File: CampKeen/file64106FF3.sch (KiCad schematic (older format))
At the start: 9 parts

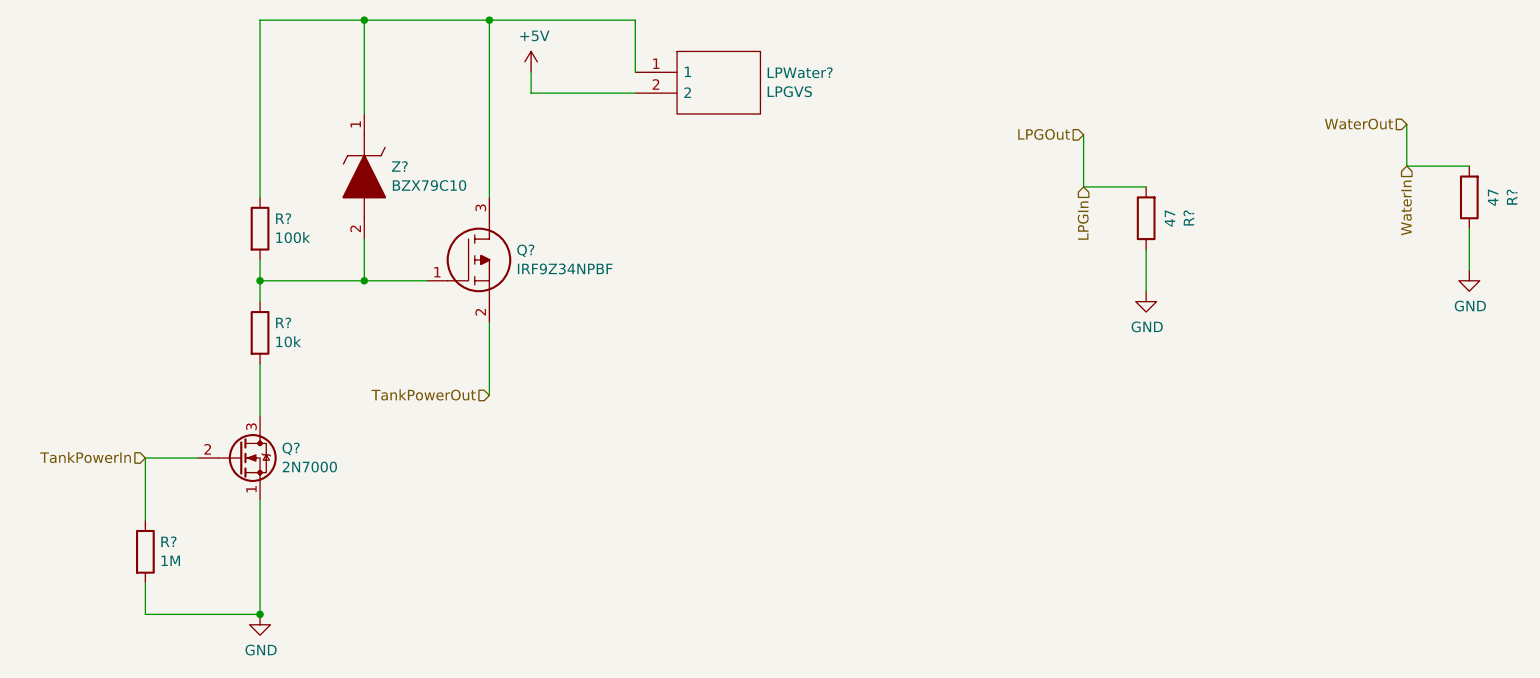
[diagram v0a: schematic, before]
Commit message: updated the pin mapping to the terms. cleaned up the Schematic. PCB placement and routing is what is left to do.
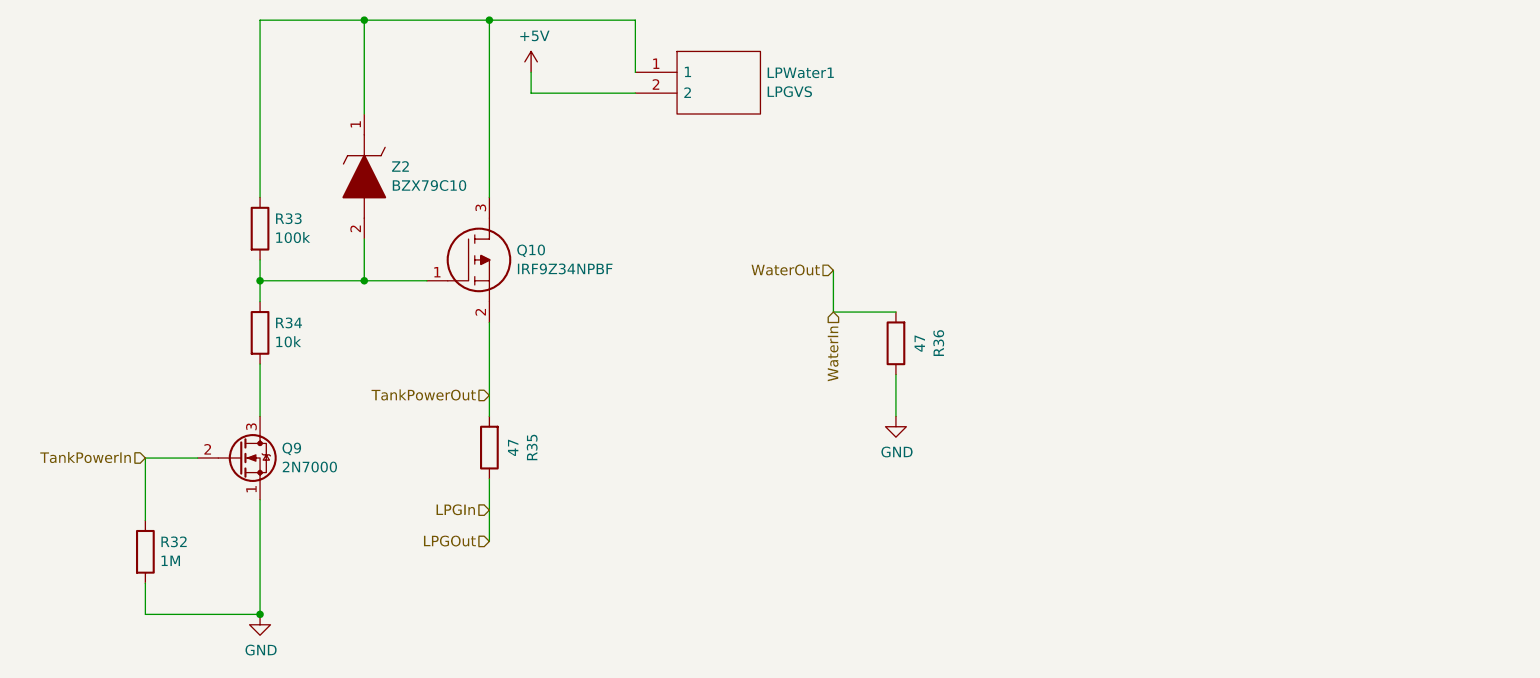
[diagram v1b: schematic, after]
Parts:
- Q10: renamed from Q?; footprint TO254P469X1042X1967-3P -> SamacSys_Parts:TO254P469X1042X1967-3P
- Z2: renamed from Z?; footprint DIOAD1068W53L380D172 -> SamacSys_Parts:DIOAD1068W53L380D172
- gave numbers to parts that had none: 7
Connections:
- net GND: no longer R35.1
- net LPGIn: now also R35.1; no longer R35.2
- net TankPowerOut: now also R35.2
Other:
- moved on the sheet: R35, R36
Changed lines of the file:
@@
 $Descr A4 11693 8268
 encoding utf-8
-Sheet 4 8
+Sheet 4 9
 Title ""
 Date ""
@@
 P 4000 2250
 AR Path="/641A2399" Ref="#PWR?"  Part="1"
-AR Path="/64106FF4/641A2399" Ref="#PWR?"  Part="1"
-F 0 "#PWR?" H 4000 2100 50  0001 C CNN
+AR Path="/64106FF4/641A2399" Ref="#PWR078"  Part="1"
+F 0 "#PWR078" H 4000 2100 50  0001 C CNN
 F 1 "+5V" H 4015 2423 50  0000 C CNN
 F 2 "" H 4000 2250 50  0001 C CNN
@@
 P 4500 2250
 AR Path="/641A23A6" Ref="LPWater?"  Part="1"
-AR Path="/64106FF4/641A23A6" Ref="LPWater?"  Part="1"
-F 0 "LPWater?" H 5128 2246 50  0000 L CNN
+AR Path="/64106FF4/641A23A6" Ref="LPWater1"  Part="1"
+F 0 "LPWater1" H 5128 2246 50  0000 L CNN
 F 1 "LPGVS" H 5128 2155 50  0000 L CNN
 F 2 "SamacSys_Parts:BK_HTC-15M" H 5150 2350 50  0001 L CNN
@@
 P 3500 3250
 AR Path="/62665296/641A23B2" Ref="Q?"  Part="1"
-AR Path="/64106FF4/641A23B2" Ref="Q?"  Part="1"
-F 0 "Q?" H 3930 3396 50  0000 L CNN
+AR Path="/64106FF4/641A23B2" Ref="Q10"  Part="1"
+F 0 "Q10" H 3930 3396 50  0000 L CNN
 F 1 "IRF9Z34NPBF" H 3930 3305 50  0000 L CNN
-F 2 "TO254P469X1042X1967-3P" H 3950 3200 50  0001 L CNN
+F 2 "SamacSys_Parts:TO254P469X1042X1967-3P" H 3950 3200 50  0001 L CNN
 F 3 "https://www.infineon.com/dgdl/irf9z34npbf.pdf?fileId=5546d462533600a40153561220af1ddd" H 3950 3100 50  0001 L CNN
 F 4 "MOSFET MOSFT PCh -55V -17A 100mOhm 23.3nC" H 3950 3000 50  0001 L CNN "Description"
@@
 P 2150 4550
 AR Path="/62665296/641A23B8" Ref="R?"  Part="1"
-AR Path="/64106FF4/641A23B8" Ref="R?"  Part="1"
-F 0 "R?" H 2220 4596 50  0000 L CNN
+AR Path="/64106FF4/641A23B8" Ref="R32"  Part="1"
+F 0 "R32" H 2220 4596 50  0000 L CNN
 F 1 "1M" H 2220 4505 50  0000 L CNN
 F 2 "Resistor_THT:R_Axial_DIN0207_L6.3mm_D2.5mm_P2.54mm_Vertical" V 2080 4550 50  0001 C CNN
@@
 P 2700 4850
 AR Path="/62665296/641A23BE" Ref="#PWR?"  Part="1"
-AR Path="/64106FF4/641A23BE" Ref="#PWR?"  Part="1"
-F 0 "#PWR?" H 2700 4600 50  0001 C CNN
+AR Path="/64106FF4/641A23BE" Ref="#PWR077"  Part="1"
+F 0 "#PWR077" H 2700 4600 50  0001 C CNN
 F 1 "GND" H 2705 4677 50  0000 C CNN
 F 2 "" H 2700 4850 50  0001 C CNN
@@
 P 2600 4100
 AR Path="/62665296/641A23C9" Ref="Q?"  Part="1"
-AR Path="/64106FF4/641A23C9" Ref="Q?"  Part="1"
-F 0 "Q?" H 2804 4146 50  0000 L CNN
+AR Path="/64106FF4/641A23C9" Ref="Q9"  Part="1"
+F 0 "Q9" H 2804 4146 50  0000 L CNN
 F 1 "2N7000" H 2804 4055 50  0000 L CNN
 F 2 "Package_TO_SOT_THT:TO-92_Inline" H 2800 4025 50  0001 L CIN
@@
 P 2700 3000
 AR Path="/62665296/641A23D0" Ref="R?"  Part="1"
-AR Path="/64106FF4/641A23D0" Ref="R?"  Part="1"
-F 0 "R?" H 2770 3046 50  0000 L CNN
+AR Path="/64106FF4/641A23D0" Ref="R33"  Part="1"
+F 0 "R33" H 2770 3046 50  0000 L CNN
 F 1 "100k" H 2770 2955 50  0000 L CNN
 F 2 "Resistor_THT:R_Axial_DIN0207_L6.3mm_D2.5mm_P2.54mm_Vertical" V 2630 3000 50  0001 C CNN
@@
 P 2700 3500
 AR Path="/62665296/641A23D6" Ref="R?"  Part="1"
-AR Path="/64106FF4/641A23D6" Ref="R?"  Part="1"
-F 0 "R?" H 2770 3546 50  0000 L CNN
+AR Path="/64106FF4/641A23D6" Ref="R34"  Part="1"
+F 0 "R34" H 2770 3546 50  0000 L CNN
 F 1 "10k" H 2770 3455 50  0000 L CNN
 F 2 "Resistor_THT:R_Axial_DIN0207_L6.3mm_D2.5mm_P2.54mm_Vertical" V 2630 3500 50  0001 C CNN
@@
 P 3200 2450
 AR Path="/62665296/641A23E2" Ref="Z?"  Part="1"
-AR Path="/64106FF4/641A23E2" Ref="Z?"  Part="1"
-F 0 "Z?" V 3454 2320 50  0000 R CNN
+AR Path="/64106FF4/641A23E2" Ref="Z2"  Part="1"
+F 0 "Z2" V 3454 2320 50  0000 R CNN
 F 1 "BZX79C10" V 3545 2320 50  0000 R CNN
-F 2 "DIOAD1068W53L380D172" H 3600 2600 50  0001 L CNN
+F 2 "SamacSys_Parts:DIOAD1068W53L380D172" H 3600 2600 50  0001 L CNN
 F 3 "https://www.fairchildsemi.com/datasheets/BZ/BZX79C10.pdf" H 3600 2500 50  0001 L CNN
 F 4 "BZX79C10, Zener Diode, 10V +/-5 500 mW 0.2A, 2-Pin DO-35" H 3600 2400 50  0001 L CNN "Description"
@@
 	3200 2000 2700 2000
 Wire Wire Line
-	3800 3800 3800 3450
-Wire Wire Line
 	3800 2000 4500 2000
 Wire Wire Line
@@
 TankPowerOut
 $Comp
-L Device:R R?
+L Device:R R35
 U 1 1 643133F3
-P 6950 2950
-F 0 "R?" V 6743 2950 50  0000 C CNN
-F 1 "47" V 6834 2950 50  0000 C CNN
-F 2 "Resistor_THT:R_Axial_DIN0207_L6.3mm_D2.5mm_P2.54mm_Vertical" V 6880 2950 50  0001 C CNN
-F 3 "~" H 6950 2950 50  0001 C CNN
-	1    6950 2950
+P 3800 4050
+F 0 "R35" V 3593 4050 50  0000 C CNN
+F 1 "47" V 3684 4050 50  0000 C CNN
+F 2 "Resistor_THT:R_Axial_DIN0207_L6.3mm_D2.5mm_P2.54mm_Vertical" V 3730 4050 50  0001 C CNN
+F 3 "~" H 3800 4050 50  0001 C CNN
+	1    3800 4050
 	-1   0    0    1
 $EndComp
 $Comp
-L power:GND #PWR?
-U 1 1 643133F9
-P 6950 3300
-F 0 "#PWR?" H 6950 3050 50  0001 C CNN
-F 1 "GND" H 6955 3127 50  0000 C CNN
-F 2 "" H 6950 3300 50  0001 C CNN
-F 3 "" H 6950 3300 50  0001 C CNN
-	1    6950 3300
-	1    0    0    -1
-$EndComp
-Wire Wire Line
-	6950 3100 6950 3300
-$Comp
-L Device:R R?
+L Device:R R36
 U 1 1 64313403
-P 8500 2850
-F 0 "R?" V 8293 2850 50  0000 C CNN
-F 1 "47" V 8384 2850 50  0000 C CNN
-F 2 "Resistor_THT:R_Axial_DIN0207_L6.3mm_D2.5mm_P2.54mm_Vertical" V 8430 2850 50  0001 C CNN
-F 3 "~" H 8500 2850 50  0001 C CNN
-	1    8500 2850
+P 5750 3550
+F 0 "R36" V 5543 3550 50  0000 C CNN
+F 1 "47" V 5634 3550 50  0000 C CNN
+F 2 "Resistor_THT:R_Axial_DIN0207_L6.3mm_D2.5mm_P2.54mm_Vertical" V 5680 3550 50  0001 C CNN
+F 3 "~" H 5750 3550 50  0001 C CNN
+	1    5750 3550
 	-1   0    0    1
 $EndComp
 $Comp
-L power:GND #PWR?
+L power:GND #PWR079
 U 1 1 64313409
-P 8500 3200
-F 0 "#PWR?" H 8500 2950 50  0001 C CNN
-F 1 "GND" H 8505 3027 50  0000 C CNN
-F 2 "" H 8500 3200 50  0001 C CNN
-F 3 "" H 8500 3200 50  0001 C CNN
-	1    8500 3200
-	1    0    0    -1
-$EndComp
-Wire Wire Line
-	8500 3000 8500 3200
-Text HLabel 6650 2800 3    50   Input ~ 0
+P 5750 3900
+F 0 "#PWR079" H 5750 3650 50  0001 C CNN
+F 1 "GND" H 5755 3727 50  0000 C CNN
+F 2 "" H 5750 3900 50  0001 C CNN
+F 3 "" H 5750 3900 50  0001 C CNN
+	1    5750 3900
+	1    0    0    -1
+$EndComp
+Wire Wire Line
+	5750 3700 5750 3900
+Text HLabel 3800 4350 0    50   Input ~ 0
 LPGIn
-Text HLabel 8200 2700 3    50   Input ~ 0
+Text HLabel 5450 3400 3    50   Input ~ 0
 WaterIn
-Text HLabel 8200 2500 0    50   Input ~ 0
+Text HLabel 5450 3200 0    50   Input ~ 0
 WaterOut
-Text HLabel 6650 2550 0    50   Input ~ 0
+Text HLabel 3800 4500 0    50   Input ~ 0
 LPGOut
 Wire Wire Line
-	6950 2800 6650 2800
-Wire Wire Line
-	6650 2550 6650 2800
-Wire Wire Line
-	8200 2500 8200 2700
-Wire Wire Line
-	8500 2700 8200 2700
+	5450 3200 5450 3400
+Wire Wire Line
+	5750 3400 5450 3400
+Wire Wire Line
+	3800 4200 3800 4500
+Wire Wire Line
+	3800 3450 3800 3900
 $EndSCHEMATC

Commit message: separated the 12 and 5 volt outputs. added another spare output.
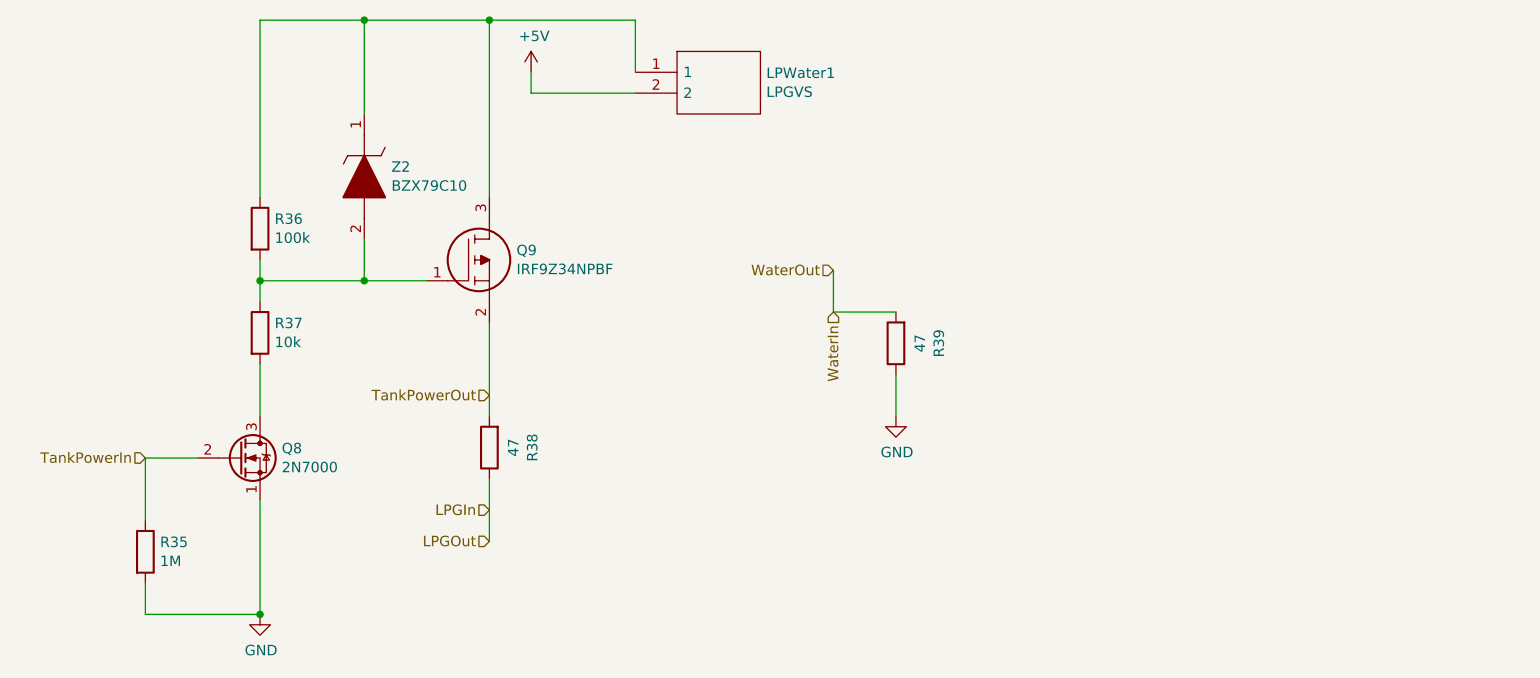
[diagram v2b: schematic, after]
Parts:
- renumbered Q9 to Q8, Q10 to Q9, R32 to R35, R33 to R36, R34 to R37, R35 to R38, R36 to R39
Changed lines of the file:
@@
 $Descr A4 11693 8268
 encoding utf-8
-Sheet 4 9
+Sheet 4 10
 Title ""
 Date ""
@@
 P 4000 2250
 AR Path="/641A2399" Ref="#PWR?"  Part="1"
-AR Path="/64106FF4/641A2399" Ref="#PWR078"  Part="1"
-F 0 "#PWR078" H 4000 2100 50  0001 C CNN
+AR Path="/64106FF4/641A2399" Ref="#PWR085"  Part="1"
+F 0 "#PWR085" H 4000 2100 50  0001 C CNN
 F 1 "+5V" H 4015 2423 50  0000 C CNN
 F 2 "" H 4000 2250 50  0001 C CNN
@@
 P 3500 3250
 AR Path="/62665296/641A23B2" Ref="Q?"  Part="1"
-AR Path="/64106FF4/641A23B2" Ref="Q10"  Part="1"
-F 0 "Q10" H 3930 3396 50  0000 L CNN
+AR Path="/64106FF4/641A23B2" Ref="Q9"  Part="1"
+F 0 "Q9" H 3930 3396 50  0000 L CNN
 F 1 "IRF9Z34NPBF" H 3930 3305 50  0000 L CNN
 F 2 "SamacSys_Parts:TO254P469X1042X1967-3P" H 3950 3200 50  0001 L CNN
@@
 P 2150 4550
 AR Path="/62665296/641A23B8" Ref="R?"  Part="1"
-AR Path="/64106FF4/641A23B8" Ref="R32"  Part="1"
-F 0 "R32" H 2220 4596 50  0000 L CNN
+AR Path="/64106FF4/641A23B8" Ref="R35"  Part="1"
+F 0 "R35" H 2220 4596 50  0000 L CNN
 F 1 "1M" H 2220 4505 50  0000 L CNN
 F 2 "Resistor_THT:R_Axial_DIN0207_L6.3mm_D2.5mm_P2.54mm_Vertical" V 2080 4550 50  0001 C CNN
@@
 P 2700 4850
 AR Path="/62665296/641A23BE" Ref="#PWR?"  Part="1"
-AR Path="/64106FF4/641A23BE" Ref="#PWR077"  Part="1"
-F 0 "#PWR077" H 2700 4600 50  0001 C CNN
+AR Path="/64106FF4/641A23BE" Ref="#PWR084"  Part="1"
+F 0 "#PWR084" H 2700 4600 50  0001 C CNN
 F 1 "GND" H 2705 4677 50  0000 C CNN
 F 2 "" H 2700 4850 50  0001 C CNN
@@
 P 2600 4100
 AR Path="/62665296/641A23C9" Ref="Q?"  Part="1"
-AR Path="/64106FF4/641A23C9" Ref="Q9"  Part="1"
-F 0 "Q9" H 2804 4146 50  0000 L CNN
+AR Path="/64106FF4/641A23C9" Ref="Q8"  Part="1"
+F 0 "Q8" H 2804 4146 50  0000 L CNN
 F 1 "2N7000" H 2804 4055 50  0000 L CNN
 F 2 "Package_TO_SOT_THT:TO-92_Inline" H 2800 4025 50  0001 L CIN
@@
 P 2700 3000
 AR Path="/62665296/641A23D0" Ref="R?"  Part="1"
-AR Path="/64106FF4/641A23D0" Ref="R33"  Part="1"
-F 0 "R33" H 2770 3046 50  0000 L CNN
+AR Path="/64106FF4/641A23D0" Ref="R36"  Part="1"
+F 0 "R36" H 2770 3046 50  0000 L CNN
 F 1 "100k" H 2770 2955 50  0000 L CNN
 F 2 "Resistor_THT:R_Axial_DIN0207_L6.3mm_D2.5mm_P2.54mm_Vertical" V 2630 3000 50  0001 C CNN
@@
 P 2700 3500
 AR Path="/62665296/641A23D6" Ref="R?"  Part="1"
-AR Path="/64106FF4/641A23D6" Ref="R34"  Part="1"
-F 0 "R34" H 2770 3546 50  0000 L CNN
+AR Path="/64106FF4/641A23D6" Ref="R37"  Part="1"
+F 0 "R37" H 2770 3546 50  0000 L CNN
 F 1 "10k" H 2770 3455 50  0000 L CNN
 F 2 "Resistor_THT:R_Axial_DIN0207_L6.3mm_D2.5mm_P2.54mm_Vertical" V 2630 3500 50  0001 C CNN
@@
 TankPowerOut
 $Comp
-L Device:R R35
+L Device:R R38
 U 1 1 643133F3
 P 3800 4050
-F 0 "R35" V 3593 4050 50  0000 C CNN
+F 0 "R38" V 3593 4050 50  0000 C CNN
 F 1 "47" V 3684 4050 50  0000 C CNN
 F 2 "Resistor_THT:R_Axial_DIN0207_L6.3mm_D2.5mm_P2.54mm_Vertical" V 3730 4050 50  0001 C CNN
@@
 $EndComp
 $Comp
-L Device:R R36
+L Device:R R39
 U 1 1 64313403
 P 5750 3550
-F 0 "R36" V 5543 3550 50  0000 C CNN
+F 0 "R39" V 5543 3550 50  0000 C CNN
 F 1 "47" V 5634 3550 50  0000 C CNN
 F 2 "Resistor_THT:R_Axial_DIN0207_L6.3mm_D2.5mm_P2.54mm_Vertical" V 5680 3550 50  0001 C CNN
@@
 $EndComp
 $Comp
-L power:GND #PWR079
+L power:GND #PWR086
 U 1 1 64313409
 P 5750 3900
-F 0 "#PWR079" H 5750 3650 50  0001 C CNN
+F 0 "#PWR086" H 5750 3650 50  0001 C CNN
 F 1 "GND" H 5755 3727 50  0000 C CNN
 F 2 "" H 5750 3900 50  0001 C CNN
